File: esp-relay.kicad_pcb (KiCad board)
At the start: 60 x 40 mm, 0 parts

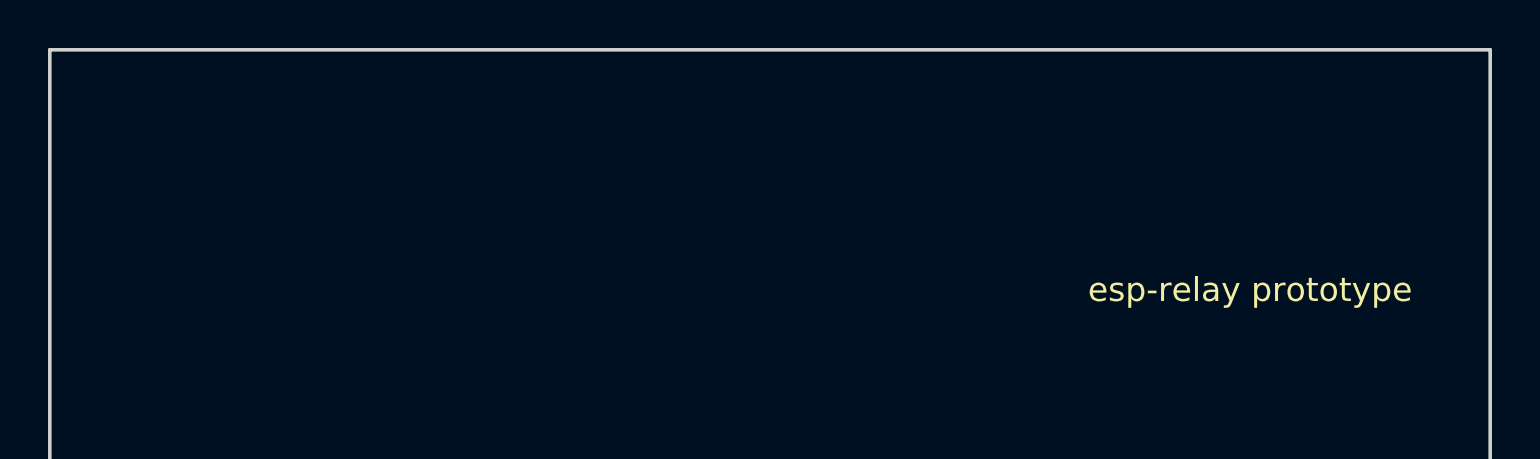
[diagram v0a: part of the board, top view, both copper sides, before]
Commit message: Fix KiCad file syntax and add valid minimal KiCad 9 project files
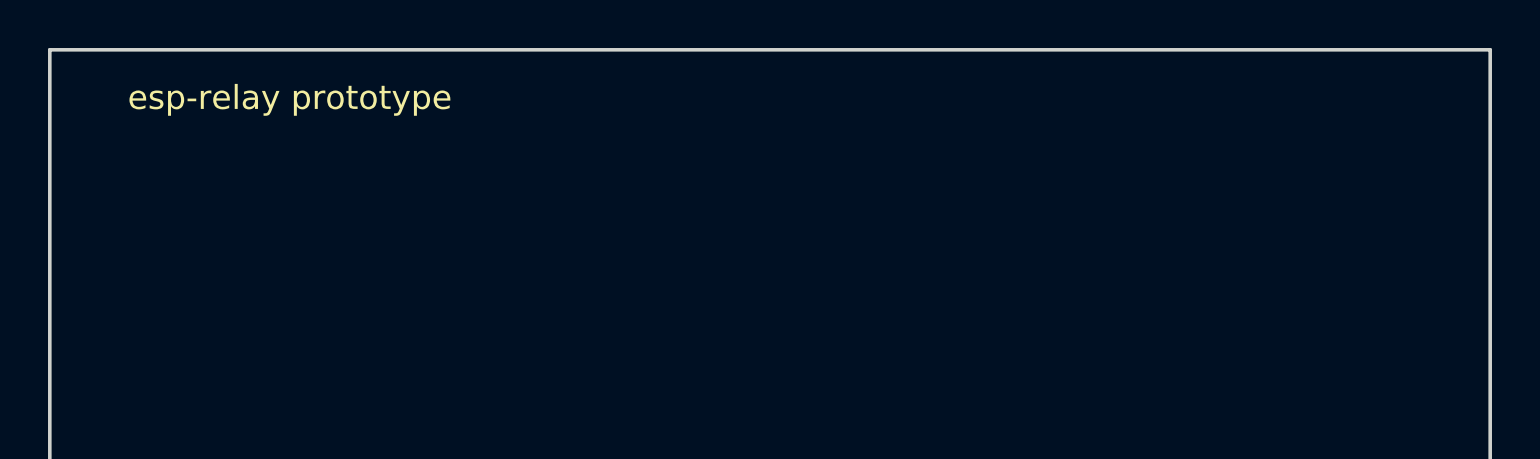
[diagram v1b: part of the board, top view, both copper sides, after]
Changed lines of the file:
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@@
   (setup (last_trace_width 0.25) (zone_clearance 0.5) (trace_clearance 0.2) (via_dia 0.8) (via_drill 0.4) (edge_width 0.15))
   (net 0 "")
-  ; Placeholder footprints and board outline for quick prototype
-  (gr_text "esp-relay prototype" (at 50 10) (layer F.SilkS) (effects (font (size 1 1) (thickness 0.15))))
+  ; Board outline for esp-relay prototype: 60mm x 40mm
   (gr_line (start 0 0) (end 60 0) (layer Edge.Cuts) (width 0.15))
   (gr_line (start 60 0) (end 60 40) (layer Edge.Cuts) (width 0.15))
   (gr_line (start 60 40) (end 0 40) (layer Edge.Cuts) (width 0.15))
   (gr_line (start 0 40) (end 0 0) (layer Edge.Cuts) (width 0.15))
-  ; Keep rest empty — use KiCad to place NodeMCU module footprint (e.g., NodeMCU-12E) and two relay footprints (Songle SRD-05VDC-SL-C) and screw terminals.
+  (gr_text "esp-relay prototype" (at 10 2) (layer F.SilkS) (effects (font (size 1 1) (thickness 0.15))))
 )
